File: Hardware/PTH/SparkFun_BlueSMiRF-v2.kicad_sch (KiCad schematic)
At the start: 38 parts, among them J1 Conn_01x06, Q1 NMOS_0.2A_50V, Q2 NMOS_0.2A_50V, SW1 SPST_Momentary_4.6x2.8mm, U1 ESP32-PICO-V3-02, U2 AP2112K-3.3

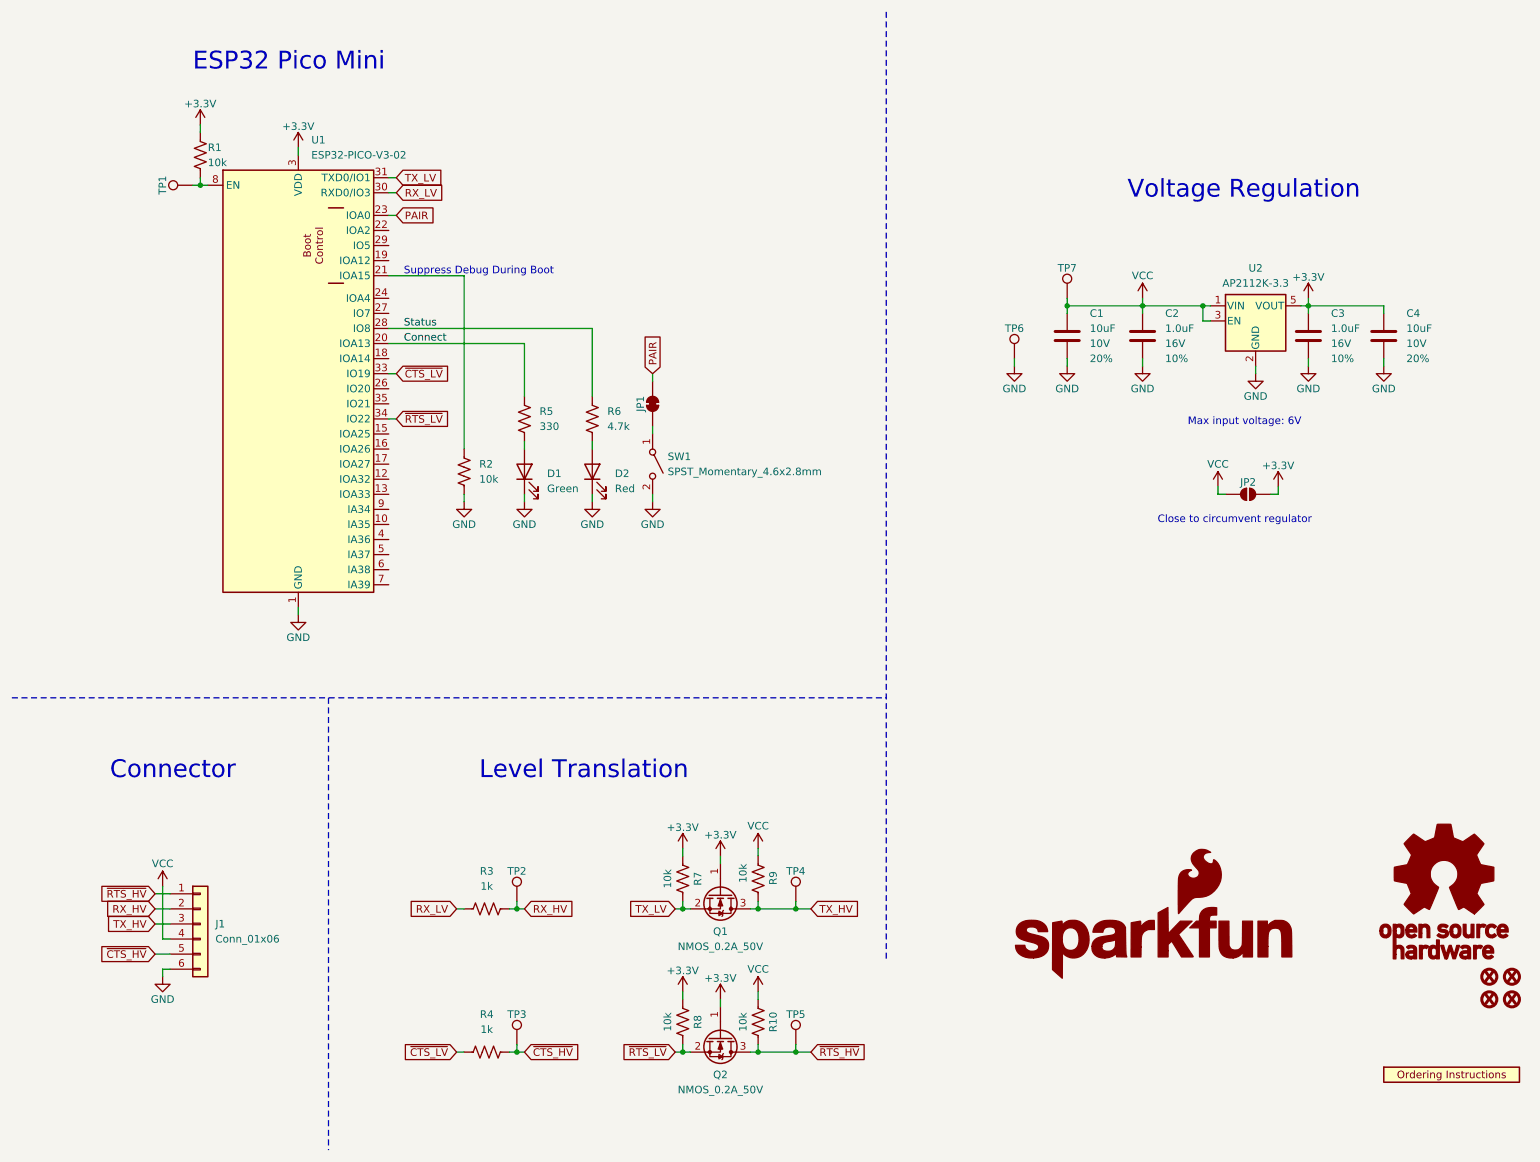
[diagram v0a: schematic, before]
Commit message: Rename Design Files
- The SMD is actually the one with the headers. =) Renaming files to reflect the boards with headers.
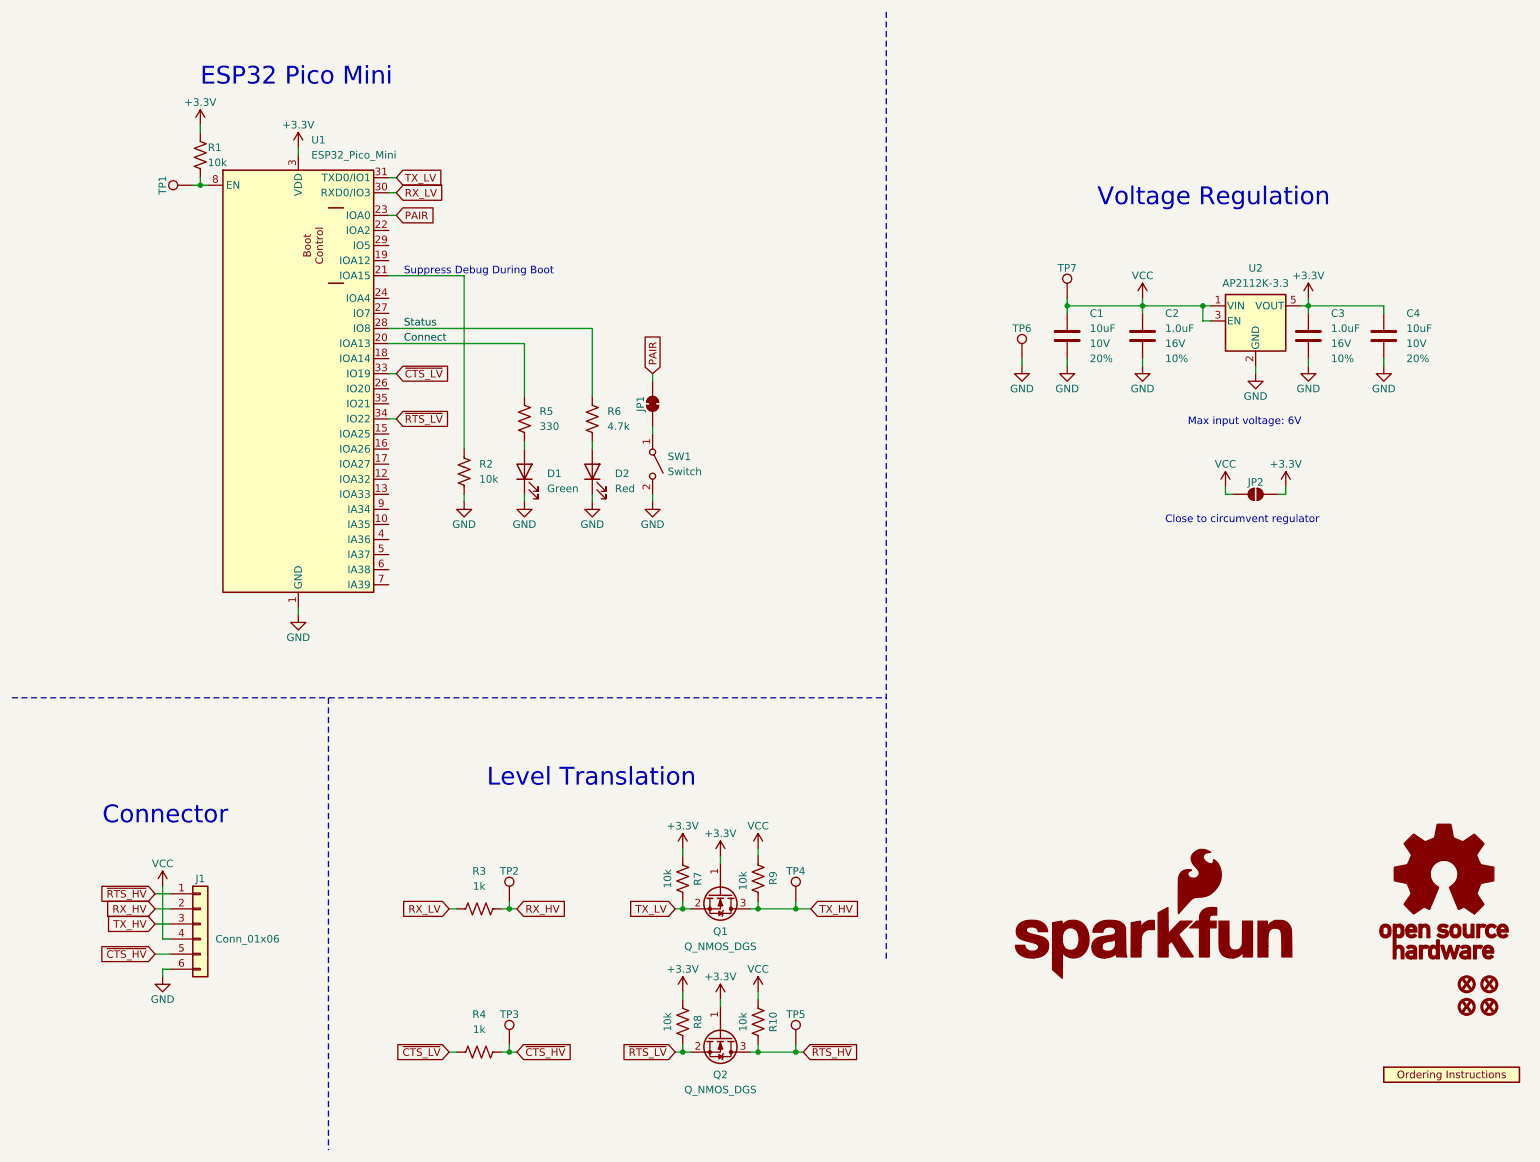
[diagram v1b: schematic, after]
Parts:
- removed J1: Conn_01x06, SparkFun-Connector:1X06-SMD_RA_MALE, symbol SparkFun-Connector:Conn_01x06_RA_SMD
- added J1: Conn_01x06, SparkFun-Connector:1X06, symbol SparkFun-Connector:Conn_01x06
- Q1, Q2: value NMOS_0.2A_50V -> Q_NMOS_DGS
- SW1: value SPST_Momentary_4.6x2.8mm -> Switch
- U1: value ESP32-PICO-V3-02 -> ESP32_Pico_Mini
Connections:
- net GND: now also J1.6 (Pin_6)
- net RX_HV: now also J1.2 (Pin_2)
- net TX_HV: now also J1.3 (Pin_3)
- net VCC: now also J1.4 (Pin_4)
- net ~{CTS_HV}: now also J1.5 (Pin_5)
- net ~{RTS_HV}: now also J1.1 (Pin_1)
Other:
- moved on the sheet: R3, R4

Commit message: Update 3D models and components to current library
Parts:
- FID1, FID2, FID3, FID4: value Fiducial_0.5 -> Fiducial_0.5mm; symbol SparkFun-Aesthetic:Fiducial_0.5 -> SparkFun-Aesthetic:Fiducial_0.5mm
- U1: footprint SparkFun-RF:ESP32-MINI -> SparkFun-RF:ESP32-PICO-MINI

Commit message: Fixing switch
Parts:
- D1: footprint SparkFun-LED:LED_0603_1608Metric -> SparkFun-LED:LED_0603_1608Metric_Green
- D2: footprint SparkFun-LED:LED_0603_1608Metric -> SparkFun-LED:LED_0603_1608Metric_Red
- J1: footprint SparkFun-Connector:1X06 -> SparkFun-Connector:1x06
- JP1: footprint SparkFun-Jumper:SMT-JUMPER_2_NC_TRACE_SILK -> SparkFun-Jumper:Jumper_2_NC_Trace
- JP2: footprint SparkFun-Jumper:SMT-JUMPER_2_NO_SILK -> SparkFun-Jumper:Jumper_2_NO
- Q1, Q2: value Q_NMOS_DGS -> BSS138; IMax (none) -> 0.2A; VMax (none) -> 50V
- SW1: value Switch -> SMD_4.6x2.8mm_h2.5mm; footprint SparkFun-Switch:Momentary_SMD_4.6x2.8mm -> SparkFun-Switch:Push_SMD_4.6x2.8mm_h2.5mm; symbol SparkFun-Switch:SPST_Momentary_4.6x2.8mm -> SparkFun-Switch:SPST_Push_SMD_4.6x2.8mm_h2.5mm
- TP1: value TestPoint -> PTH; footprint SparkFun-Connector:1X01 -> SparkFun-Connector:1x01
- TP2, TP3, TP4, TP5, TP6, TP7: value TestPoint_0.75mm -> 0.75mm
- U1: value ESP32_Pico_Mini -> ESP32-PICO-V3-02
- U2: Imax (none) -> 600mA; Iq (none) -> 55µA; VMax (none) -> 6V
- U3: footprint SparkFun-Aesthetic:ORDERING_INSTRUCTIONS -> SparkFun-Aesthetic:Ordering_Instructions
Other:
- moved on the sheet: R2, R3, R4, R5, R6
